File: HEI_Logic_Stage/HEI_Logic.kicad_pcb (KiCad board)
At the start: 4 copper layers, 61.5 x 77.7 mm, 99 parts, among them J1 RJ_{1}, J2 RJ_{2}, J3 Tag-Connect, J4 Conn_02x10_Odd_Even, J5 430450813_Molex, SW1 SW_SPST, SW2 SW_Push, U1 5V_Converter_R-78E5.0-0.5, U2 5V_Converter_R-78E5.0-0.5, U3 B1203XT-1WR3, U4 ADM3058EBRIZ, U5 STM32F334C8T6, U6 LM4132-Q1 SOT-2, U7 CD40109BQNSRQ1, U8 TMH 1212S

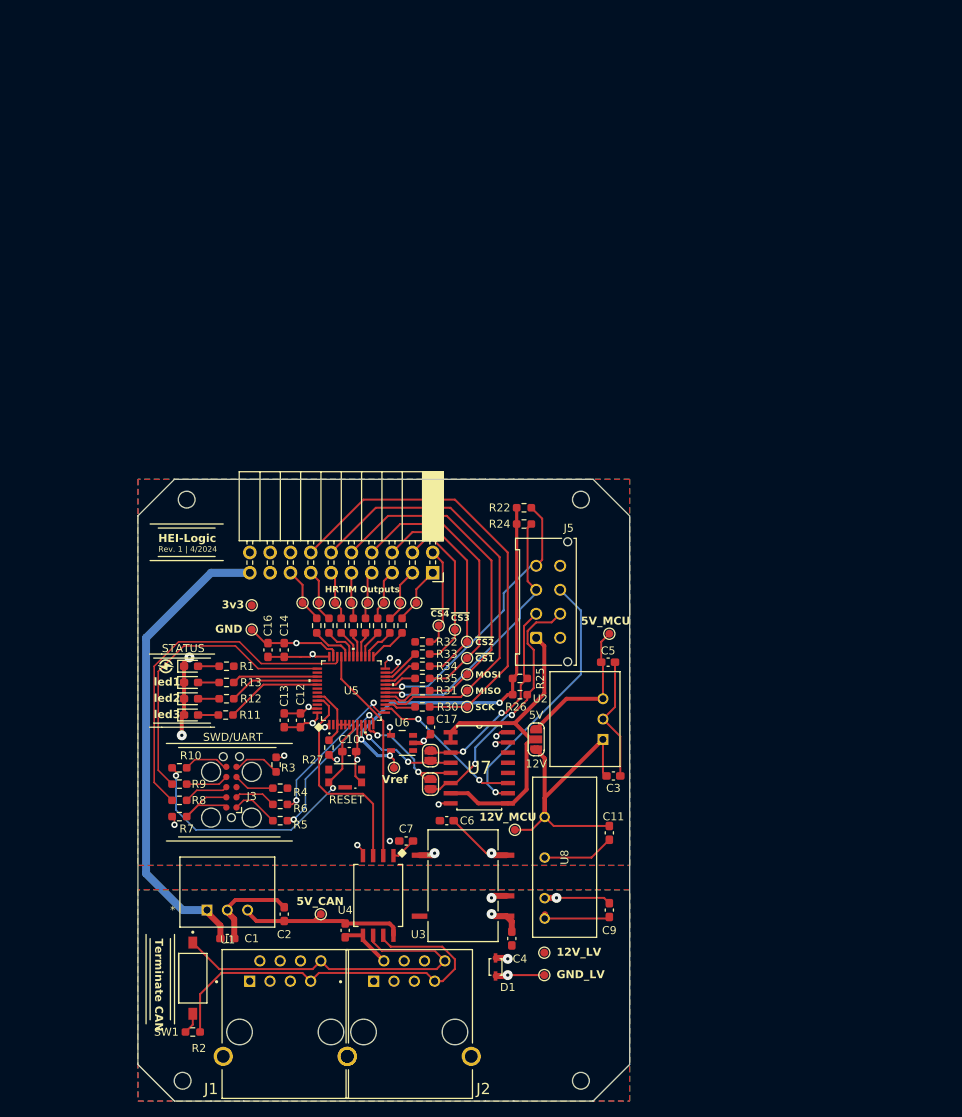
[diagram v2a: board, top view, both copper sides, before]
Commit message: vertical logic stage complete
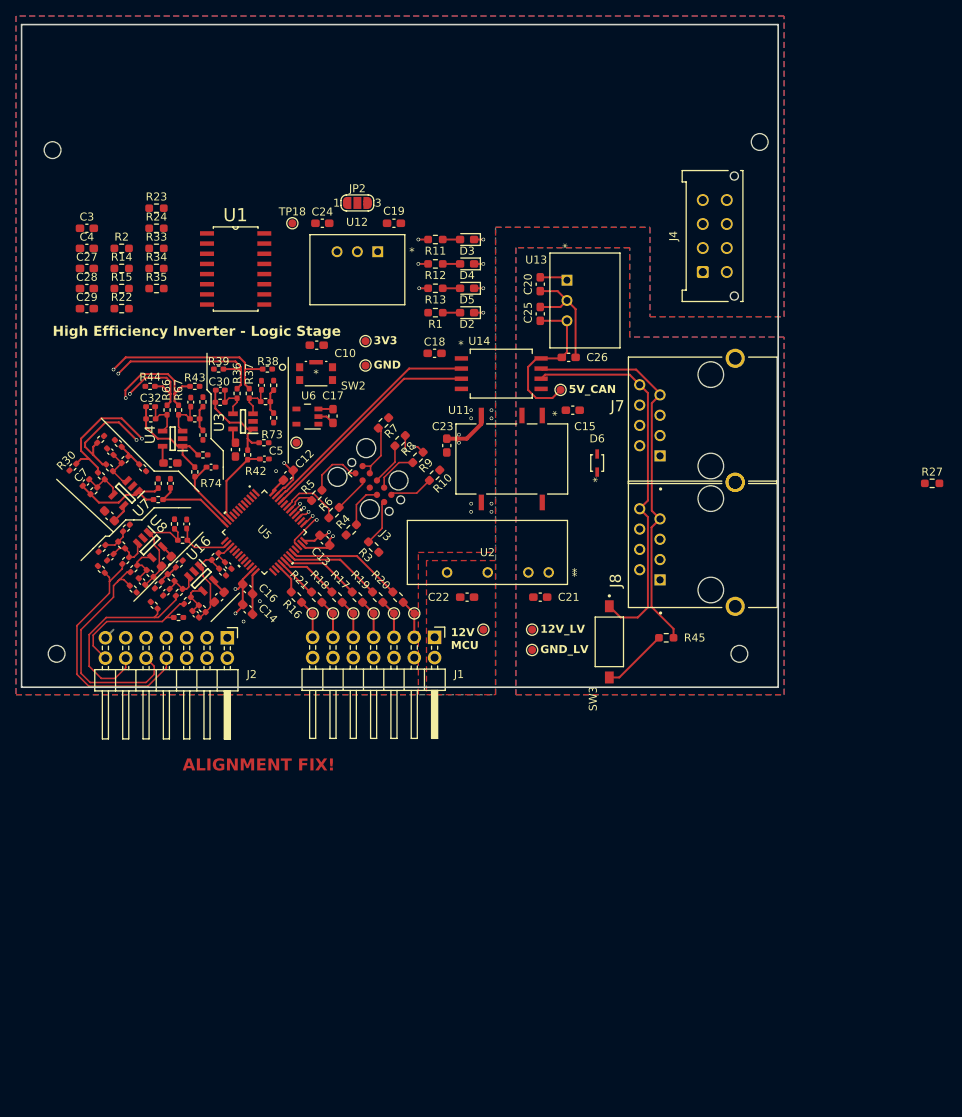
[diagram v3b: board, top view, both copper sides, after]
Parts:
- removed D1: 12V_TVS_ESD12VD3B-TP, GTSR_KiCAD_Footprints:ESD12VD3B-TP
- removed G***: LOGO, LOGO
- removed J5: 430450813_Molex, Connector_Molex:Molex_Micro-Fit_3.0_43045-0812_2x04_P3.00mm_Vertical
- removed JP1: Jumper_3_Open, Jumper:SolderJumper-3_P1.3mm_Open_RoundedPad1.0x1.5mm_NumberLabels
- removed JP4, JP5: Jumper_2_Open, Jumper:SolderJumper-2_P1.3mm_Open_RoundedPad1.0x1.5mm
- removed SW1: SW_SPST, GTSR_KiCAD_Footprints:SW_DS04-254-1-01BK-SMT
- removed TP10, TP12, TP13, TP14, TP22, TP23, TP3, TP4, TP5, TP6, TP7, TP8, TP9: Test_Point, TestPoint:TestPoint_Pad_D1.0mm
- added C15: 2.2uF, Capacitor_SMD:C_0603_1608Metric_Pad1.08x0.95mm_HandSolder, F.Cu at (88.9, 66.5)
- added C18: 0.1uF, Capacitor_SMD:C_0603_1608Metric_Pad1.08x0.95mm_HandSolder, F.Cu at (71.6, 59.4)
- added C19: 10uF, Capacitor_SMD:C_0603_1608Metric_Pad1.08x0.95mm_HandSolder, F.Cu at (66.5, 43.2)
- added C20: 10uF, Capacitor_SMD:C_0603_1608Metric_Pad1.08x0.95mm_HandSolder, F.Cu at (84.8, 50.8)
- added C21: 1uF, Capacitor_SMD:C_0603_1608Metric_Pad1.08x0.95mm_HandSolder, F.Cu at (84.8, 89.9)
- added C22: 1uF, Capacitor_SMD:C_0603_1608Metric_Pad1.08x0.95mm_HandSolder, F.Cu at (75.7, 89.9)
- added C23: 10uF, Capacitor_SMD:C_0603_1608Metric_Pad1.08x0.95mm_HandSolder, F.Cu at (73.2, 71.0)
- added C24: 10uF, Capacitor_SMD:C_0603_1608Metric_Pad1.08x0.95mm_HandSolder, F.Cu at (57.6, 43.2)
- added C25: 10uF, Capacitor_SMD:C_0603_1608Metric_Pad1.08x0.95mm_HandSolder, F.Cu at (84.8, 54.5)
- added C26: 0.1uF, Capacitor_SMD:C_0603_1608Metric_Pad1.08x0.95mm_HandSolder, F.Cu at (88.4, 59.9)
- added C27: 0.1uF, Capacitor_SMD:C_0603_1608Metric_Pad1.08x0.95mm_HandSolder, F.Cu at (28.2, 48.8)
- added C28: 0.1uF, Capacitor_SMD:C_0603_1608Metric_Pad1.08x0.95mm_HandSolder, F.Cu at (28.2, 51.3)
- added C29: 0.1uF, Capacitor_SMD:C_0603_1608Metric_Pad1.08x0.95mm_HandSolder, F.Cu at (28.2, 53.8)
- added C30: 0, Capacitor_SMD:C_0402_1005Metric_Pad0.74x0.62mm_HandSolder, F.Cu at (44.8, 64.0)
- added C31: 0, Capacitor_SMD:C_0402_1005Metric_Pad0.74x0.62mm_HandSolder, F.Cu at (50.0, 63.4)
- added C32: 0, Capacitor_SMD:C_0402_1005Metric_Pad0.74x0.62mm_HandSolder, F.Cu at (36.1, 66.1)
- added C33: 33p, Capacitor_SMD:C_0402_1005Metric_Pad0.74x0.62mm_HandSolder, F.Cu at (43.7, 73.7)
- added C34: 0, Capacitor_SMD:C_0402_1005Metric_Pad0.74x0.62mm_HandSolder, F.Cu at (38.1, 89.3)
- added C35: 0, Capacitor_SMD:C_0402_1005Metric_Pad0.74x0.62mm_HandSolder, F.Cu at (35.1, 88.0)
- added C36: 0, Capacitor_SMD:C_0402_1005Metric_Pad0.74x0.62mm_HandSolder, F.Cu at (41.1, 65.5)
- added C37: 0, Capacitor_SMD:C_0402_1005Metric_Pad0.74x0.62mm_HandSolder, F.Cu at (31.1, 84.9)
- added C38: 33p, Capacitor_SMD:C_0402_1005Metric_Pad0.74x0.62mm_HandSolder, F.Cu at (40.6, 80.8)
- added C39: 0.1uF, Capacitor_SMD:C_0603_1608Metric_Pad1.08x0.95mm_HandSolder, F.Cu at (31.0, 79.8)
- added C40: 0.1uF, Capacitor_SMD:C_0603_1608Metric_Pad1.08x0.95mm_HandSolder, F.Cu at (38.1, 85.4)
- added C41: 33p, Capacitor_SMD:C_0402_1005Metric_Pad0.74x0.62mm_HandSolder, F.Cu at (45.8, 86.0)
- added D6: 12V_TVS_ESD12VD3B-TP, GTSR_KiCAD_Footprints:ESD12VD3B-TP, F.Cu at (91.9, 73.2)
- added J7: RJ_{1}, GTSR_KiCAD_Footprints:ASSMANN_A-2004-2-4-LPS-N-R, F.Cu at (106.2, 67.8)
- added J8: RJ_{2}, GTSR_KiCAD_Footprints:ASSMANN_A-2004-2-4-LPS-N-R, F.Cu at (106.2, 83.3)
- added JP2: Jumper_3_Open, Jumper:SolderJumper-3_P1.3mm_Open_RoundedPad1.0x1.5mm_NumberLabels, F.Cu at (62.0, 40.6)
- added R23: X, Resistor_SMD:R_0603_1608Metric_Pad0.98x0.95mm_HandSolder, F.Cu at (36.9, 41.3)
- added R28: 10k, Resistor_SMD:R_0402_1005Metric_Pad0.72x0.64mm_HandSolder, F.Cu at (36.6, 90.9)
- added R29: 10k, Resistor_SMD:R_0402_1005Metric_Pad0.72x0.64mm_HandSolder, F.Cu at (29.9, 70.2)
- added R36: 40k, Resistor_SMD:R_0402_1005Metric_Pad0.72x0.64mm_HandSolder, F.Cu at (46.9, 64.5)
- added R37: 40k, Resistor_SMD:R_0402_1005Metric_Pad0.72x0.64mm_HandSolder, F.Cu at (48.5, 64.5)
- added R38: 10k, Resistor_SMD:R_0402_1005Metric_Pad0.72x0.64mm_HandSolder, F.Cu at (50.7, 61.4)
- added R39: 10k, Resistor_SMD:R_0402_1005Metric_Pad0.72x0.64mm_HandSolder, F.Cu at (44.6, 61.4)
- added R40: 25k, Resistor_SMD:R_0402_1005Metric_Pad0.72x0.64mm_HandSolder, F.Cu at (50.5, 65.5)
- added R41: 30k, Resistor_SMD:R_0402_1005Metric_Pad0.72x0.64mm_HandSolder, F.Cu at (44.8, 65.6)
- added R42: 120, Resistor_SMD:R_0402_1005Metric_Pad0.72x0.64mm_HandSolder, F.Cu at (48.3, 72.1)
- added R43: 10k, Resistor_SMD:R_0402_1005Metric_Pad0.72x0.64mm_HandSolder, F.Cu at (41.7, 63.6)
- added R44: 10k, Resistor_SMD:R_0402_1005Metric_Pad0.72x0.64mm_HandSolder, F.Cu at (36.1, 63.6)
- added R45: 120, Resistor_SMD:R_0603_1608Metric_Pad0.98x0.95mm_HandSolder, F.Cu at (100.6, 95.0)
- added R46: 10k, Resistor_SMD:R_0402_1005Metric_Pad0.72x0.64mm_HandSolder, F.Cu at (35.1, 73.7)
- added R47: 25k, Resistor_SMD:R_0402_1005Metric_Pad0.72x0.64mm_HandSolder, F.Cu at (32.9, 72.7)
- added R48: 30k, Resistor_SMD:R_0402_1005Metric_Pad0.72x0.64mm_HandSolder, F.Cu at (29.0, 76.6)
- added R49: 10k, Resistor_SMD:R_0402_1005Metric_Pad0.72x0.64mm_HandSolder, F.Cu at (32.1, 70.7)
- added R50: 10k, Resistor_SMD:R_0402_1005Metric_Pad0.72x0.64mm_HandSolder, F.Cu at (37.1, 75.7)
- added R51: 120, Resistor_SMD:R_0402_1005Metric_Pad0.72x0.64mm_HandSolder, F.Cu at (37.1, 77.7)
- added R52: 10k, Resistor_SMD:R_0402_1005Metric_Pad0.72x0.64mm_HandSolder, F.Cu at (30.0, 86.4)
- added R53: 25k, Resistor_SMD:R_0402_1005Metric_Pad0.72x0.64mm_HandSolder, F.Cu at (41.7, 67.6)
- added R54: 10k, Resistor_SMD:R_0402_1005Metric_Pad0.72x0.64mm_HandSolder, F.Cu at (34.0, 88.9)
- added R55: 40k, Resistor_SMD:R_0402_1005Metric_Pad0.72x0.64mm_HandSolder, F.Cu at (34.0, 86.4)
- added R56: 10k, Resistor_SMD:R_0402_1005Metric_Pad0.72x0.64mm_HandSolder, F.Cu at (51.5, 67.5)
- added R57: 10k, Resistor_SMD:R_0402_1005Metric_Pad0.72x0.64mm_HandSolder, F.Cu at (51.5, 63.4)
- added R58: 40k, Resistor_SMD:R_0402_1005Metric_Pad0.72x0.64mm_HandSolder, F.Cu at (33.0, 85.3)
- added R59: 10k, Resistor_SMD:R_0402_1005Metric_Pad0.72x0.64mm_HandSolder, F.Cu at (33.1, 81.3)
- added R60: 25k, Resistor_SMD:R_0402_1005Metric_Pad0.72x0.64mm_HandSolder, F.Cu at (32.5, 83.4)
- added R61: 30k, Resistor_SMD:R_0402_1005Metric_Pad0.72x0.64mm_HandSolder, F.Cu at (36.1, 87.0)
- added R62: 10k, Resistor_SMD:R_0402_1005Metric_Pad0.72x0.64mm_HandSolder, F.Cu at (39.6, 92.5)
- added R63: 40k, Resistor_SMD:R_0402_1005Metric_Pad0.72x0.64mm_HandSolder, F.Cu at (40.7, 90.3)
- added R64: 40k, Resistor_SMD:R_0402_1005Metric_Pad0.72x0.64mm_HandSolder, F.Cu at (39.7, 89.3)
- added R65: 10k, Resistor_SMD:R_0402_1005Metric_Pad0.72x0.64mm_HandSolder, F.Cu at (39.7, 85.8)
- added R66: 40k, Resistor_SMD:R_0402_1005Metric_Pad0.72x0.64mm_HandSolder, F.Cu at (38.2, 66.5)
- added R67: 40k, Resistor_SMD:R_0402_1005Metric_Pad0.72x0.64mm_HandSolder, F.Cu at (39.6, 66.5)
- added R68: 10k, Resistor_SMD:R_0402_1005Metric_Pad0.72x0.64mm_HandSolder, F.Cu at (30.1, 83.8)
- added R69: 30k, Resistor_SMD:R_0402_1005Metric_Pad0.72x0.64mm_HandSolder, F.Cu at (36.2, 67.6)
- added R70: 10k, Resistor_SMD:R_0402_1005Metric_Pad0.72x0.64mm_HandSolder, F.Cu at (42.7, 72.1)
- added R71: 25k, Resistor_SMD:R_0402_1005Metric_Pad0.72x0.64mm_HandSolder, F.Cu at (38.7, 87.5)
- added R72: 30k, Resistor_SMD:R_0402_1005Metric_Pad0.72x0.64mm_HandSolder, F.Cu at (42.6, 91.4)
- added R73: 10k, Resistor_SMD:R_0402_1005Metric_Pad0.72x0.64mm_HandSolder, F.Cu at (50.3, 70.6)
- added R74: 120, Resistor_SMD:R_0402_1005Metric_Pad0.72x0.64mm_HandSolder, F.Cu at (41.7, 74.3)
- added R75: 10k, Resistor_SMD:R_0402_1005Metric_Pad0.72x0.64mm_HandSolder, F.Cu at (39.1, 80.8)
- added R76: 120, Resistor_SMD:R_0402_1005Metric_Pad0.72x0.64mm_HandSolder, F.Cu at (40.1, 82.8)
- added R77: 10k, Resistor_SMD:R_0402_1005Metric_Pad0.72x0.64mm_HandSolder, F.Cu at (37.1, 88.4)
- added R78: 10k, Resistor_SMD:R_0402_1005Metric_Pad0.72x0.64mm_HandSolder, F.Cu at (45.1, 86.8)
- added R79: 120, Resistor_SMD:R_0402_1005Metric_Pad0.72x0.64mm_HandSolder, F.Cu at (44.2, 84.8)
- added SW3: SW_SPST, GTSR_KiCAD_Footprints:SW_DS04-254-1-01BK-SMT, F.Cu at (93.5, 95.5)
- added TP24: Test_Point, TestPoint:TestPoint_Pad_D1.0mm, F.Cu at (61.5, 91.9)
- added TP25: Test_Point, TestPoint:TestPoint_Pad_D1.0mm, F.Cu at (64.0, 91.9)
- added TP26: Test_Point, TestPoint:TestPoint_Pad_D1.0mm, F.Cu at (66.5, 91.9)
- added TP27: Test_Point, TestPoint:TestPoint_Pad_D1.0mm, F.Cu at (69.1, 91.9)
- added U11: B1203XT-1WR3, GTSR_KiCAD_Footprints:B_XT-1WR3_MNS-M, F.Cu at (81.3, 72.6)
- added U12: 5V_Converter_R-78E5.0-0.5, GTSR_KiCAD_Footprints:R-78E5.0-0.5, F.Cu at (62.0, 49.0)
- added U13: 5V_Converter_R-78E5.0-0.5, GTSR_KiCAD_Footprints:R-78E5.0-0.5, F.Cu at (90.4, 52.8)
- added U14: ADM3058EBRIZ, GTSR_KiCAD_Footprints:8-SOIC_ADM3058EBRIZ, F.Cu at (80.3, 62.0)
- added U16: TLV9051IDBVR, HEI_Logic:SOT95P280X145-5N, F.Cu at (42.5, 87.6)
- C1, C2, C3: value 10uF -> 0.1uF
- C11: value 1uF -> 0.1uF
- C17: value 0.1uF -> 4.7u
- C4: value 2.2uF -> 0.1uF
- C5: value 10uF -> 33p; footprint Capacitor_SMD:C_0603_1608Metric_Pad1.08x0.95mm_HandSolder -> Capacitor_SMD:C_0402_1005Metric_Pad0.74x0.62mm_HandSolder
- C6: value 10uF -> 0; footprint Capacitor_SMD:C_0603_1608Metric_Pad1.08x0.95mm_HandSolder -> Capacitor_SMD:C_0402_1005Metric_Pad0.74x0.62mm_HandSolder
- C7, C8: value 0.1uF -> 0; footprint Capacitor_SMD:C_0603_1608Metric_Pad1.08x0.95mm_HandSolder -> Capacitor_SMD:C_0402_1005Metric_Pad0.74x0.62mm_HandSolder
- C9: value 1uF -> 33p; footprint Capacitor_SMD:C_0603_1608Metric_Pad1.08x0.95mm_HandSolder -> Capacitor_SMD:C_0402_1005Metric_Pad0.74x0.62mm_HandSolder
- J1: value RJ_{1} -> Conn_02x07_Odd_Even; footprint GTSR_KiCAD_Footprints:ASSMANN_A-2004-2-4-LPS-N-R -> Connector_PinHeader_2.54mm:PinHeader_2x07_P2.54mm_Horizontal
- J2: value RJ_{2} -> Conn_02x07_Odd_Even; footprint GTSR_KiCAD_Footprints:ASSMANN_A-2004-2-4-LPS-N-R -> Connector_PinHeader_2.54mm:PinHeader_2x07_P2.54mm_Horizontal
- J4: value Conn_02x10_Odd_Even -> 430450813_Molex; footprint Connector_PinSocket_2.54mm:PinSocket_2x10_P2.54mm_Horizontal -> Connector_Molex:Molex_Micro-Fit_3.0_43045-0812_2x04_P3.00mm_Vertical
- R14: value 330 -> X
- R2: value 120 -> X
- R22, R24: value X -> 330
- R25, R26: value X -> 10k; footprint Resistor_SMD:R_0603_1608Metric_Pad0.98x0.95mm_HandSolder -> Resistor_SMD:R_0402_1005Metric_Pad0.72x0.64mm_HandSolder
- R30: value 330 -> 10k; footprint Resistor_SMD:R_0603_1608Metric_Pad0.98x0.95mm_HandSolder -> Resistor_SMD:R_0402_1005Metric_Pad0.72x0.64mm_HandSolder
- R31, R32: value 330 -> 40k; footprint Resistor_SMD:R_0603_1608Metric_Pad0.98x0.95mm_HandSolder -> Resistor_SMD:R_0402_1005Metric_Pad0.72x0.64mm_HandSolder
- U1: value 5V_Converter_R-78E5.0-0.5 -> CD40109BQNSRQ1; footprint GTSR_KiCAD_Footprints:R-78E5.0-0.5 -> HEI_Logic:SOIC127P780X200-16N
- U2: value 5V_Converter_R-78E5.0-0.5 -> TMH 1212S; footprint GTSR_KiCAD_Footprints:R-78E5.0-0.5 -> HEI_Logic:TMH SINGLE_TRP
- U3: value B1203XT-1WR3 -> TLV9051IDBVR; footprint GTSR_KiCAD_Footprints:B_XT-1WR3_MNS-M -> HEI_Logic:SOT95P280X145-5N
- U4: value ADM3058EBRIZ -> TLV9051IDBVR; footprint GTSR_KiCAD_Footprints:8-SOIC_ADM3058EBRIZ -> HEI_Logic:SOT95P280X145-5N
- U5: footprint GTSR_KiCAD_Footprints:LQFP48-7x7mm -> HEI_Logic:LQFP48-7x7mm
- U7: value CD40109BQNSRQ1 -> TLV9051IDBVR; footprint GTSR_KiCAD_Footprints:SOIC127P780X200-16N -> HEI_Logic:SOT95P280X145-5N
- U8: value TMH 1212S -> TLV9051IDBVR; footprint GTSR_KiCAD_Footprints:TMH SINGLE_TRP -> HEI_Logic:SOT95P280X145-5N
- moved H3 119.5 mm to (112.3, 33.0)
- moved C4 101.3 mm to (28.2, 46.3), turned to 0 degrees
- moved R2 98.4 mm to (32.5, 46.3), turned to 0 degrees
- moved C3 95.0 mm to (28.2, 43.8)
- moved R27 82.3 mm to (133.8, 75.7), turned to 0 degrees
- moved H4 79.2 mm to (23.9, 34.0)
- moved U1 77.9 mm to (46.8, 48.9)
- moved C9 76.5 mm to (38.6, 75.7)
- moved C11 71.7 mm to (38.6, 73.2), turned to 0 degrees
- moved H1 71.7 mm to (109.7, 97.0)
- moved D3 68.7 mm to (75.7, 45.2), turned to 180 degrees
- moved U8 67.9 mm to (36.1, 83.4), turned to -45 degrees
- moved C8 66.7 mm to (31.1, 71.7), turned to -45 degrees
- moved R11 65.0 mm to (71.7, 45.2), turned to 180 degrees
- moved D4 64.4 mm to (75.7, 48.3), turned to 180 degrees
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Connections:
- net /10kSaver renamed /Unused
- C1 pad 1: /12V_LV -> +3V3
- C1 pad 2: /GND_LV -> GND
- C11 pad 1: /12V_MCU -> +3V3
- C2 pad 1: /5V_CAN -> +3V3
- C2 pad 2: /GND_LV -> GND
- C3 pad 1: /12V_MCU -> +3V3
- C4 pad 1: /12V_LV -> V_Hall
- C4 pad 2: /GND_LV -> GND
- C5 pad 1: /5V_MCU -> /PhA_I
- C6 pad 1: +3V3 -> /Control & Motor Interface/E-
- C6 pad 2: GND -> /Control & Motor Interface/Eo
- C7 pad 1: GND -> /Control & Motor Interface/C-
- C7 pad 2: +3V3 -> /Control & Motor Interface/Co
- C8 pad 1: /GND_LV -> GND
- C8 pad 2: /5V_CAN -> /Control & Motor Interface/C+
- C9 pad 1: /12V_LV -> /PhC_I
- C9 pad 2: /GND_LV -> GND
- J1 pad 1: /12V_LV -> GND
- J1 pad 2: /GND_LV -> +12V_MCU
- J1 pad 3: /12V_LV -> /HRTIM_B2
- J1 pad 4: /GND_LV -> unconnected-(J1-Pin_4-Pad4)
- J1 pad 5: /12V_LV -> /HRTIM_B1
- J1 pad 6: /GND_LV -> unconnected-(J1-Pin_6-Pad6)
- J1 pad 7: /CANH -> /HRTIM_A2
- J1 pad 8: /CANL -> unconnected-(J1-Pin_8-Pad8)
- J2 pad 1: /12V_LV -> GND
- J2 pad 2: /GND_LV -> +5V
- J2 pad 3: /12V_LV -> /Control & Motor Interface/PhC_IsenseRef
- J2 pad 4: /GND_LV -> unconnected-(J2-Pin_4-Pad4)
- J2 pad 5: /12V_LV -> /Control & Motor Interface/PhC_Isense+
- J2 pad 6: /GND_LV -> unconnected-(J2-Pin_6-Pad6)
- J2 pad 7: /CANH -> /Control & Motor Interface/PhB_IsenseRef
- J2 pad 8: /CANL -> /Control & Motor Interface/DCIsense+
- J4 pad 1: /HRTIM_C1 -> V_Hall
- J4 pad 2: /~{CS4} -> Net-(J4-Pad2)
- J4 pad 3: /HRTIM_C2 -> Net-(J4-Pad3)
- J4 pad 4: /~{CS3} -> Net-(J4-Pad4)
- J4 pad 5: /HRTIM_D1 -> GND
- J4 pad 6: /~{CS2} -> Net-(J4-Pad6)
- J4 pad 7: /HRTIM_D2 -> Net-(J4-Pad7)
- J4 pad 8: /~{CS1} -> Net-(J4-Pad8)
- R14 pad 1: /HRTIM_C1_r -> /Vref
- R14 pad 2: /HRTIM_C1 -> Net-(J4-Pad4)
- R15 pad 1: /HRTIM_C2_r -> /Control & Motor Interface/HallIN1
- R15 pad 2: /HRTIM_C2 -> Net-(J4-Pad2)
- R2 pad 1: /CANH -> /Vref
- R2 pad 2: Net-(SW1-B) -> Net-(J4-Pad8)
- R22 pad 1: /Vref -> Net-(J4-Pad6)
- R22 pad 2: /TIN2 -> /Control & Motor Interface/HallIN2
- R24 pad 1: /Vref -> Net-(J4-Pad7)
- R24 pad 2: /TIN1 -> /Control & Motor Interface/HallIN3
- R25 pad 1: /Vref -> Net-(R25-Pad1)
- R25 pad 2: /HallIN1/TIN3 -> /Vref
- R26 pad 1: /Vref -> GND
- R26 pad 2: /HallIN2/TIN4 -> Net-(R25-Pad1)
- R30 pad 1: /SCK -> GND
- R30 pad 2: /SCK_r -> /Control & Motor Interface/PhC_IsenseRef
- R31 pad 1: /MOSI -> /Control & Motor Interface/PhC_IsenseRef
- R31 pad 2: /MOSI_r -> /Control & Motor Interface/C-
- R32 pad 1: /~{CS4} -> /Control & Motor Interface/PhC_Isense+
- R32 pad 2: /~{CS4}_r -> /Control & Motor Interface/C+
- R33 pad 1: /~{CS3} -> Net-(J4-Pad8)
- R33 pad 2: /~{CS3}_r -> /TIN3
- R34 pad 1: /~{CS2} -> Net-(J4-Pad3)
- R34 pad 2: /~{CS2}_r -> /TIN1
- R35 pad 1: /~{CS1} -> Net-(J4-Pad4)
- R35 pad 2: /~{CS1}_r -> /TIN2
- TP1 pad 1: /HRTIM_C1 -> +12V_LV
- TP15 pad 1: /~{CS4} -> +3V3
- TP16 pad 1: /~{CS1} -> GND
- TP17 pad 1: /~{CS2} -> +12V_MCU
- TP18 pad 1: /~{CS3} -> +5V
- TP19 pad 1: /SCK -> +5V_CAN
- TP2 pad 1: /HRTIM_C2 -> GND_LV
- TP20 pad 1: /MISO -> /HRTIM_D1
- TP21 pad 1: /MOSI -> /HRTIM_D2
- U1 pad 1: /12V_LV -> V_Hall
- U1 pad 2: /GND_LV -> V_Hall
- U1 pad 3: /5V_CAN -> /Control & Motor Interface/HallIN1
- U2 pad 1: /12V_MCU -> +12V_LV
- U2 pad 2: GND -> GND_LV
- U3 pad 1: /GND_LV -> /Control & Motor Interface/Ao
- U3 pad 2: /12V_LV -> GND
- U3 pad 4: GND -> /Control & Motor Interface/A-
- U4 pad 1: +3V3 -> /Control & Motor Interface/Bo
- U4 pad 2: /CAN_TX -> GND
- U4 pad 3: /CAN_RX -> /Control & Motor Interface/B+
- U4 pad 4: GND -> /Control & Motor Interface/B-
- U4 pad 5: /GND_LV -> +3V3
- U5 pad 10: /HallIN1_3v3/ADC -> /PhA_I
- U5 pad 11: /HallIN2_3v3/ADC -> /PhB_I
- U5 pad 12: /UART_TX -> /PhC_I
- U5 pad 13: /UART_RX -> unconnected-(U5-PA3-Pad13)
- U5 pad 14: /HallIN3_3v3 -> /DCI
- U5 pad 15: /SCK_r -> /DCV
- U5 pad 16: /MISO -> /TIN1
- U5 pad 17: /MOSI_r -> /TIN2
- U5 pad 18: /TIN1 -> /HallIN1_3v3
- U5 pad 19: /TIN2 -> /HallIN2_3v3
- U5 pad 20: /~{CS1}_r -> /TIN3
- U5 pad 21: /~{CS2}_r -> /HallIN3_3v3
- U5 pad 22: /~{CS3}_r -> unconnected-(U5-PB11-Pad22)
- U5 pad 25: /HRTIM_C1_r -> unconnected-(U5-PB12-Pad25)
- U5 pad 26: /HRTIM_C2_r -> unconnected-(U5-PB13-Pad26)
- U5 pad 33: /CAN_TX -> unconnected-(U5-PA12-Pad33)
- U5 pad 38: /~{CS4}_r -> unconnected-(U5-PA15-Pad38)
- U5 pad 42: unconnected-(U5-PB6-Pad42) -> /UART_TX
- U5 pad 43: unconnected-(U5-PB7-Pad43) -> /UART_RX
- U5 pad 46: unconnected-(U5-PB9-Pad46) -> /CAN_TX
- U7 pad 1: /V_Hall -> /Control & Motor Interface/Co
- U7 pad 2: /V_Hall -> GND
- U7 pad 3: /HallIN1/TIN3 -> /Control & Motor Interface/C+
- U7 pad 4: /HallIN1_3v3/ADC -> /Control & Motor Interface/C-
- U7 pad 5: /HallIN2_3v3/ADC -> +3V3
- U8 pad 1: /12V_LV -> /Control & Motor Interface/Do
- U8 pad 2: /GND_LV -> GND
- U8 pad 4: GND -> /Control & Motor Interface/D-
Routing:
- net /GND_LV: track 96.2 -> 0.00 mm, vias 3 -> 0
- net /12V_LV: track 71.2 -> 0.00 mm, vias 2 -> 0
- net /Control & Motor Interface/PhA_Isense+: track 0.00 -> 57.0 mm, vias 0 -> 1
- net /SCK: track 56.2 -> 0.00 mm
- net /MISO: track 55.4 -> 0.00 mm
- net /Control & Motor Interface/PhA_IsenseRef: track 0.00 -> 55.2 mm, vias 0 -> 1
- net /Vref: track 54.0 -> 0.00 mm, vias 3 -> 0
- net /CANH: track 51.3 -> 0.00 mm
- net /Power & CAN/CANH: track 0.00 -> 49.1 mm
- net /Power & CAN/CANL: track 0.00 -> 48.1 mm
- net GND: track 80.9 -> 33.9 mm, vias 15 -> 14
- net /Control & Motor Interface/PhB_Isense+: track 0.00 -> 45.8 mm, vias 0 -> 1
- net /Control & Motor Interface/PhC_IsenseRef: track 0.00 -> 45.0 mm, vias 0 -> 1
- net /CANL: track 44.9 -> 0.00 mm
- net /Control & Motor Interface/PhB_IsenseRef: track 0.00 -> 44.0 mm, vias 0 -> 1
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- added copper zone on F.Cu, net +12V_LV
- added copper zone on In2.Cu, net +12V_LV
- added copper zone on F.Cu, net +12V_MCU
- added copper zone on In2.Cu, net +12V_MCU
- added copper zone on In2.Cu, net +3V3
- added copper zone on B.Cu, net GND
- added copper zone on B.Cu, net GND_LV
- added copper zone on In1.Cu, net GND_LV
- removed copper zone on B.Cu, net +3V3
- removed copper zone on B.Cu, net /12V_LV
- removed copper zone on F.Cu, net /12V_LV
- removed copper zone on In1.Cu, net /GND_LV
- removed copper zone on In2.Cu, net /GND_LV
- removed copper zone on In2.Cu, net GND
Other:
- board size 61.5 x 77.7 mm -> 94.6 x 82.8 mm
- board text added: "12V MCU"
- board text added: "3V3"
- board text added: "ALIGNMENT FIX!"
- board text added: "High Efficiency Inverter - Logic Stage"
- board text removed: "12V_MCU"
- board text removed: "3v3"
- board text removed: "5V_MCU"
- board text removed: "HEI-Logic"
- board text removed: "HRTIM Outputs"
- board text removed: "MISO"
- board text removed: "MOSI"
- board text removed: "RESET"
- board text removed: "Rev. 1 | 4/2024"
- board text removed: "SCK"
- board text removed: "STATUS"
- board text removed: "SWD/UART"
- board text removed: "Terminate CAN"
- board text removed: "Vref"
- board text removed: "led1"
- board text removed: "led2"
- board text removed: "led3"
- board text removed: "~{CS1}"
- board text removed: "~{CS2}"
- board text removed: "~{CS3}"
- board text removed: "~{CS4}"
